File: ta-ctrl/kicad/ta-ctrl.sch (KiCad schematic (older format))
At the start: 6 parts

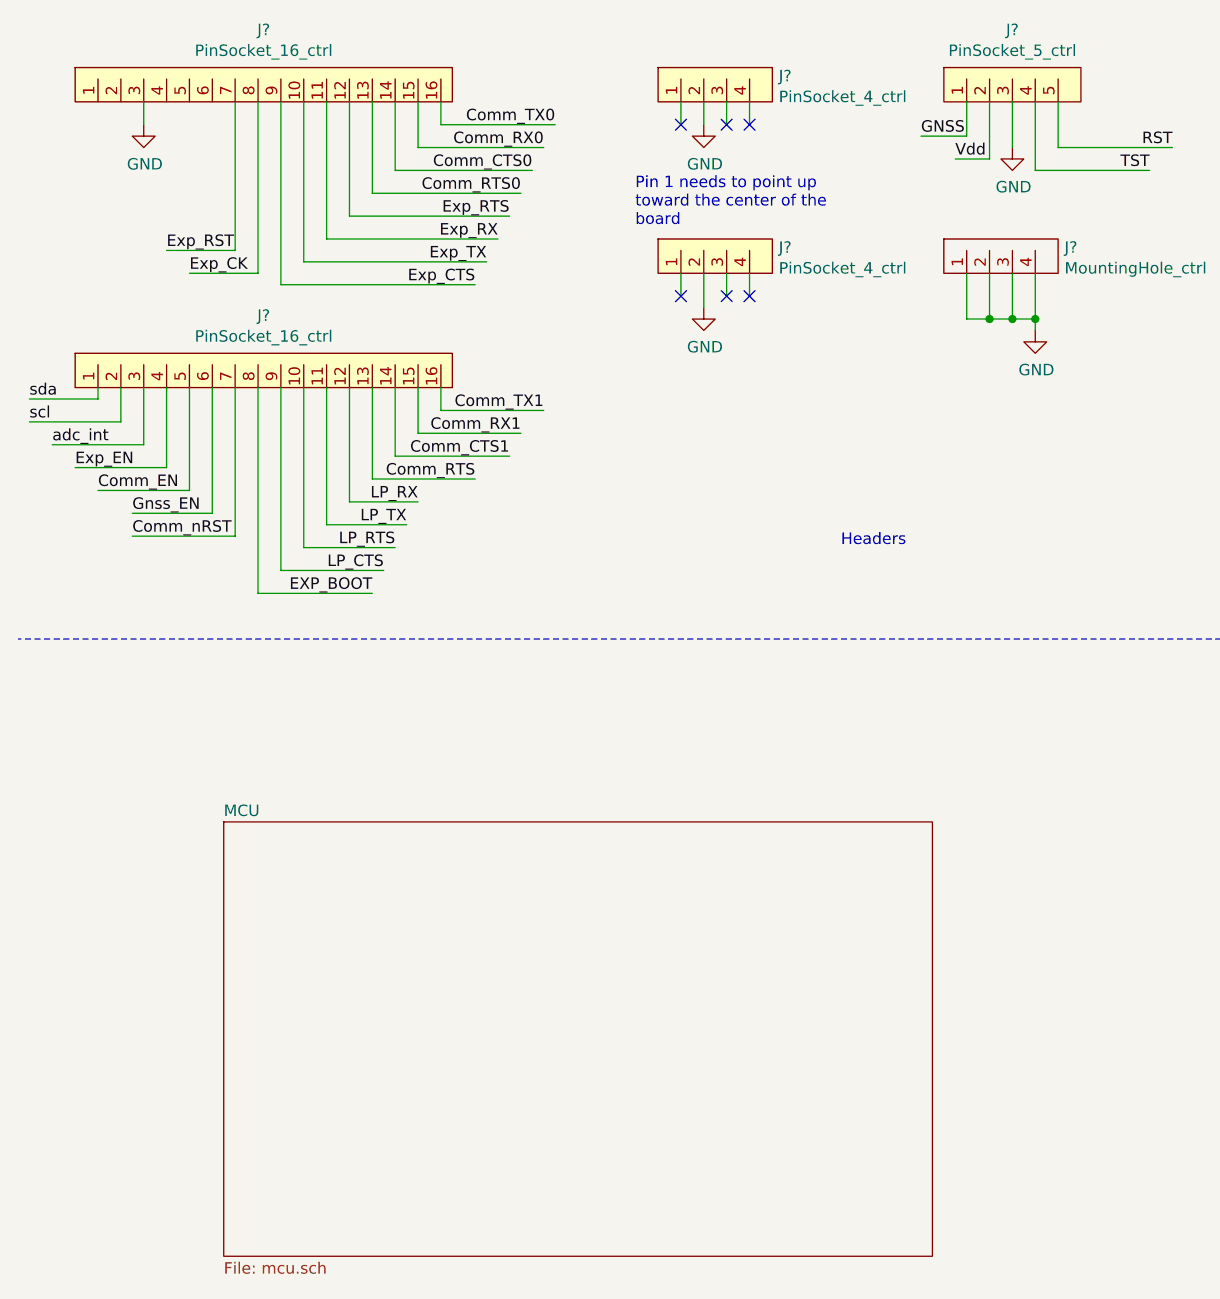
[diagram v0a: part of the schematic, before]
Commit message: Added initial pin assignments
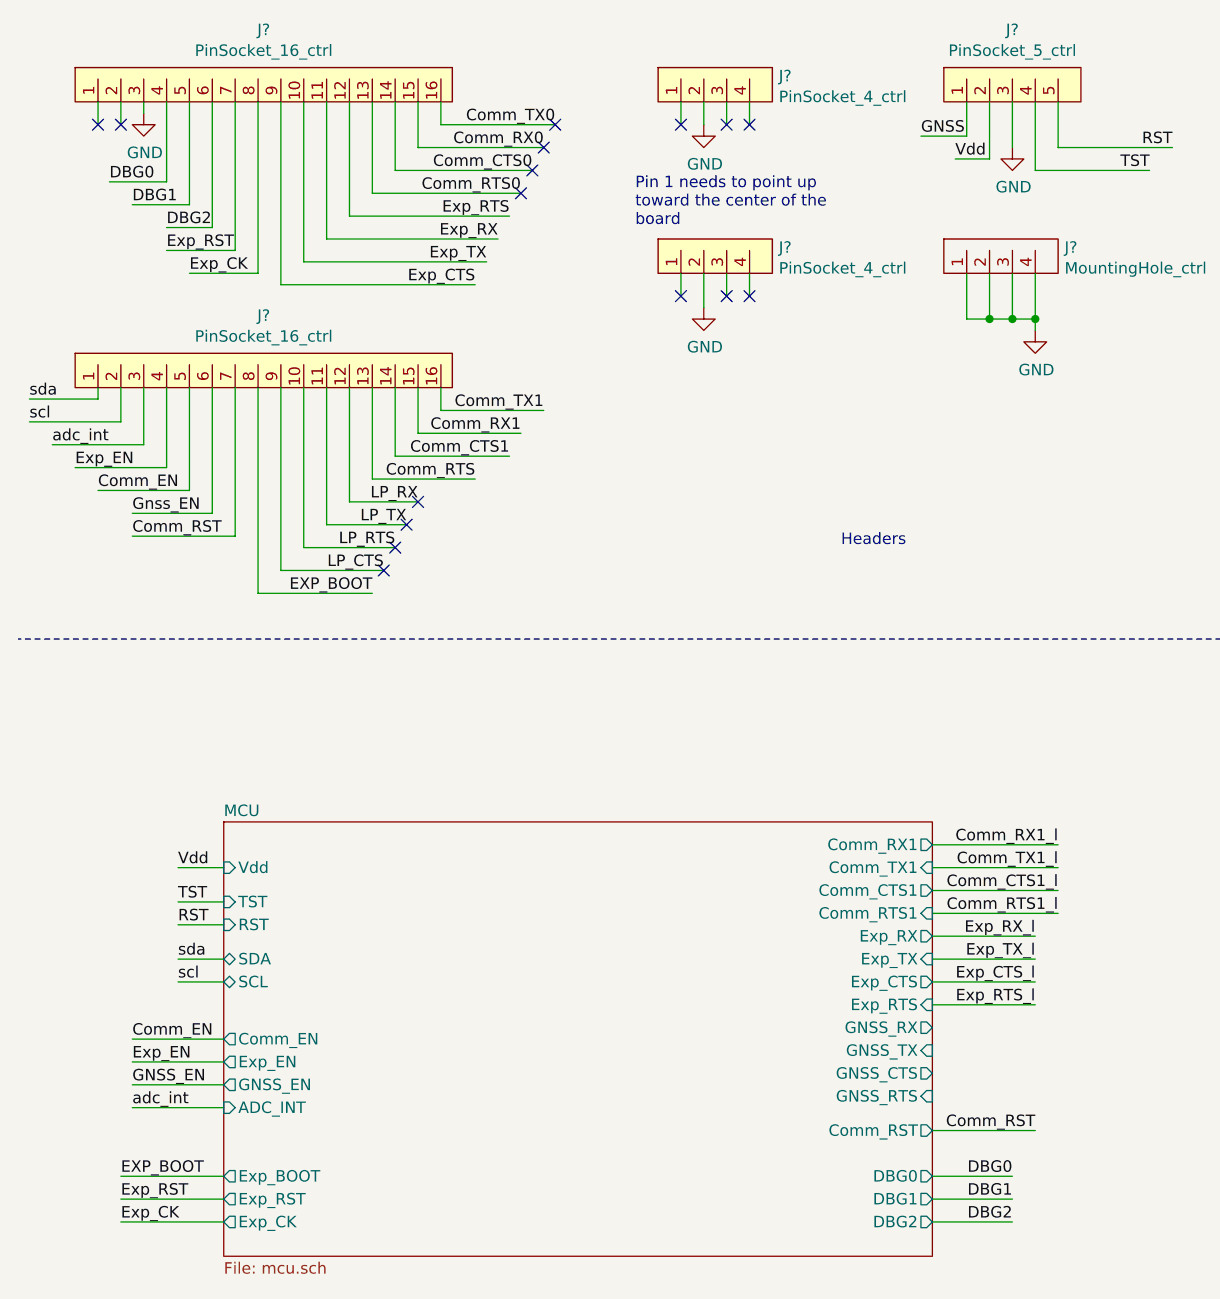
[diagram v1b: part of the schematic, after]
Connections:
- net DBG0: now reaches J?.4
- net DBG1: now reaches J?.5
- net DBG2: now reaches J?.6
- net Comm_nRST renamed Comm_RST
- no-connect marks 6 -> 16
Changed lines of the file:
@@
 	3400 850  3400 950
 Wire Wire Line
-	1050 850  1050 950
+	1050 850  1050 900
 $Comp
 L power:GND #PWR?
 U 1 1 5F17F9A1
-P 1050 950
-F 0 "#PWR?" H 1050 700 50  0001 C CNN
-F 1 "GND" H 1055 777 50  0000 C CNN
-F 2 "" H 1050 950 50  0001 C CNN
-F 3 "" H 1050 950 50  0001 C CNN
-	1    1050 950
+P 1050 900
+F 0 "#PWR?" H 1050 650 50  0001 C CNN
+F 1 "GND" H 1055 727 50  0000 C CNN
+F 2 "" H 1050 900 50  0001 C CNN
+F 3 "" H 1050 900 50  0001 C CNN
+	1    1050 900
 	1    0    0    -1
 $EndComp
@@
 	1450 2100 1450 2750
 Text Label 1000 2750 0    50   ~ 0
-Comm_nRST
+Comm_RST
 Wire Wire Line
 	1000 2750 1450 2750
@@
 Text Label 1250 1600 0    50   ~ 0
 Exp_CK
-Text Label 1150 1500 0    50   ~ 0
-Exp_RST
 Wire Wire Line
 	1550 850  1550 1600
@@
 F0 "MCU" 50
 F1 "mcu.sch" 50
+F2 "Vdd" I L 1400 4200 50
+F3 "TST" I L 1400 4350 50
+F4 "RST" I L 1400 4450 50
+F5 "Comm_RX1" O R 4500 4100 50
+F6 "Comm_TX1" I R 4500 4200 50
+F7 "Exp_RX" O R 4500 4500 50
+F8 "Exp_TX" I R 4500 4600 50
+F9 "Exp_CTS" O R 4500 4700 50
+F10 "Exp_RTS" I R 4500 4800 50
+F11 "GNSS_RX" O R 4500 4900 50
+F12 "GNSS_TX" I R 4500 5000 50
+F13 "GNSS_CTS" O R 4500 5100 50
+F14 "GNSS_RTS" I R 4500 5200 50
+F15 "SDA" B L 1400 4600 50
+F16 "SCL" B L 1400 4700 50
+F17 "Comm_CTS1" O R 4500 4300 50
+F18 "Comm_RTS1" I R 4500 4400 50
+F19 "Comm_EN" O L 1400 4950 50
+F20 "Exp_EN" O L 1400 5050 50
+F21 "GNSS_EN" O L 1400 5150 50
+F22 "ADC_INT" I L 1400 5250 50
+F23 "DBG1" O R 4500 5650 50
+F24 "DBG2" O R 4500 5750 50
+F25 "DBG0" O R 4500 5550 50
+F26 "Exp_BOOT" O L 1400 5550 50
+F27 "Comm_RST" O R 4500 5350 50
+F28 "Exp_CK" O L 1400 5750 50
+F29 "Exp_RST" O L 1400 5650 50
 $EndSheet
 $Sheet
@@
 F1 "sensors.sch" 50
 $EndSheet
+NoConn ~ 2850 950
+NoConn ~ 2800 1050
+NoConn ~ 2750 1150
+NoConn ~ 2700 1250
+NoConn ~ 2250 2600
+NoConn ~ 2200 2700
+NoConn ~ 2150 2800
+NoConn ~ 2100 2900
+Text Label 1200 4200 0    50   ~ 0
+Vdd
+Wire Wire Line
+	1200 4200 1400 4200
+Text Label 5050 4100 2    50   ~ 0
+Comm_RX1_l
+Wire Wire Line
+	4500 4100 5050 4100
+Text Label 5050 4200 2    50   ~ 0
+Comm_TX1_l
+Wire Wire Line
+	4500 4200 5050 4200
+Text Label 5050 4300 2    50   ~ 0
+Comm_CTS1_l
+Text Label 5050 4400 2    50   ~ 0
+Comm_RTS1_l
+Text Label 4950 4500 2    50   ~ 0
+Exp_RX_l
+Text Label 4950 4600 2    50   ~ 0
+Exp_TX_l
+Wire Wire Line
+	4500 4300 5050 4300
+Wire Wire Line
+	4500 4400 5050 4400
+Wire Wire Line
+	4500 4500 4950 4500
+Wire Wire Line
+	4500 4600 4950 4600
+Text Label 4950 4700 2    50   ~ 0
+Exp_CTS_l
+Text Label 4950 4800 2    50   ~ 0
+Exp_RTS_l
+Wire Wire Line
+	4500 4800 4950 4800
+Wire Wire Line
+	4500 4700 4950 4700
+Text Label 1200 4350 0    50   ~ 0
+TST
+Text Label 1200 4450 0    50   ~ 0
+RST
+Text Label 1200 4600 0    50   ~ 0
+sda
+Text Label 1200 4700 0    50   ~ 0
+scl
+Text Label 1000 4950 0    50   ~ 0
+Comm_EN
+Text Label 1000 5050 0    50   ~ 0
+Exp_EN
+Text Label 1000 5150 0    50   ~ 0
+GNSS_EN
+Wire Wire Line
+	1000 4950 1400 4950
+Wire Wire Line
+	1000 5050 1400 5050
+Wire Wire Line
+	1000 5150 1400 5150
+Wire Wire Line
+	1200 4350 1400 4350
+Wire Wire Line
+	1200 4450 1400 4450
+Wire Wire Line
+	1200 4600 1400 4600
+Wire Wire Line
+	1200 4700 1400 4700
+Text Label 1000 5250 0    50   ~ 0
+adc_int
+Wire Wire Line
+	1000 5250 1400 5250
+Text Label 950  5550 0    50   ~ 0
+EXP_BOOT
+Wire Wire Line
+	950  5550 1400 5550
+Text Label 950  5650 0    50   ~ 0
+Exp_RST
+Wire Wire Line
+	950  5650 1400 5650
+Text Label 950  5750 0    50   ~ 0
+Exp_CK
+Wire Wire Line
+	950  5750 1400 5750
+NoConn ~ 850  950
+NoConn ~ 950  950
+Wire Wire Line
+	850  850  850  950
+Wire Wire Line
+	950  850  950  950
+Text Label 900  1200 0    50   ~ 0
+DBG0
+Text Label 1000 1300 0    50   ~ 0
+DBG1
+Text Label 1150 1400 0    50   ~ 0
+DBG2
+Text Label 1150 1500 0    50   ~ 0
+Exp_RST
+Wire Wire Line
+	1350 850  1350 1400
+Wire Wire Line
+	1350 1400 1150 1400
+Wire Wire Line
+	1250 850  1250 1300
+Wire Wire Line
+	1250 1300 1000 1300
+Wire Wire Line
+	1150 850  1150 1200
+Wire Wire Line
+	1150 1200 900  1200
+Wire Wire Line
+	4500 5350 4950 5350
+Text Label 4950 5350 2    50   ~ 0
+Comm_RST
+Text Label 4850 5550 2    50   ~ 0
+DBG0
+Text Label 4850 5650 2    50   ~ 0
+DBG1
+Text Label 4850 5750 2    50   ~ 0
+DBG2
+Wire Wire Line
+	4500 5550 4850 5550
+Wire Wire Line
+	4500 5650 4850 5650
+Wire Wire Line
+	4500 5750 4850 5750
 $EndSCHEMATC

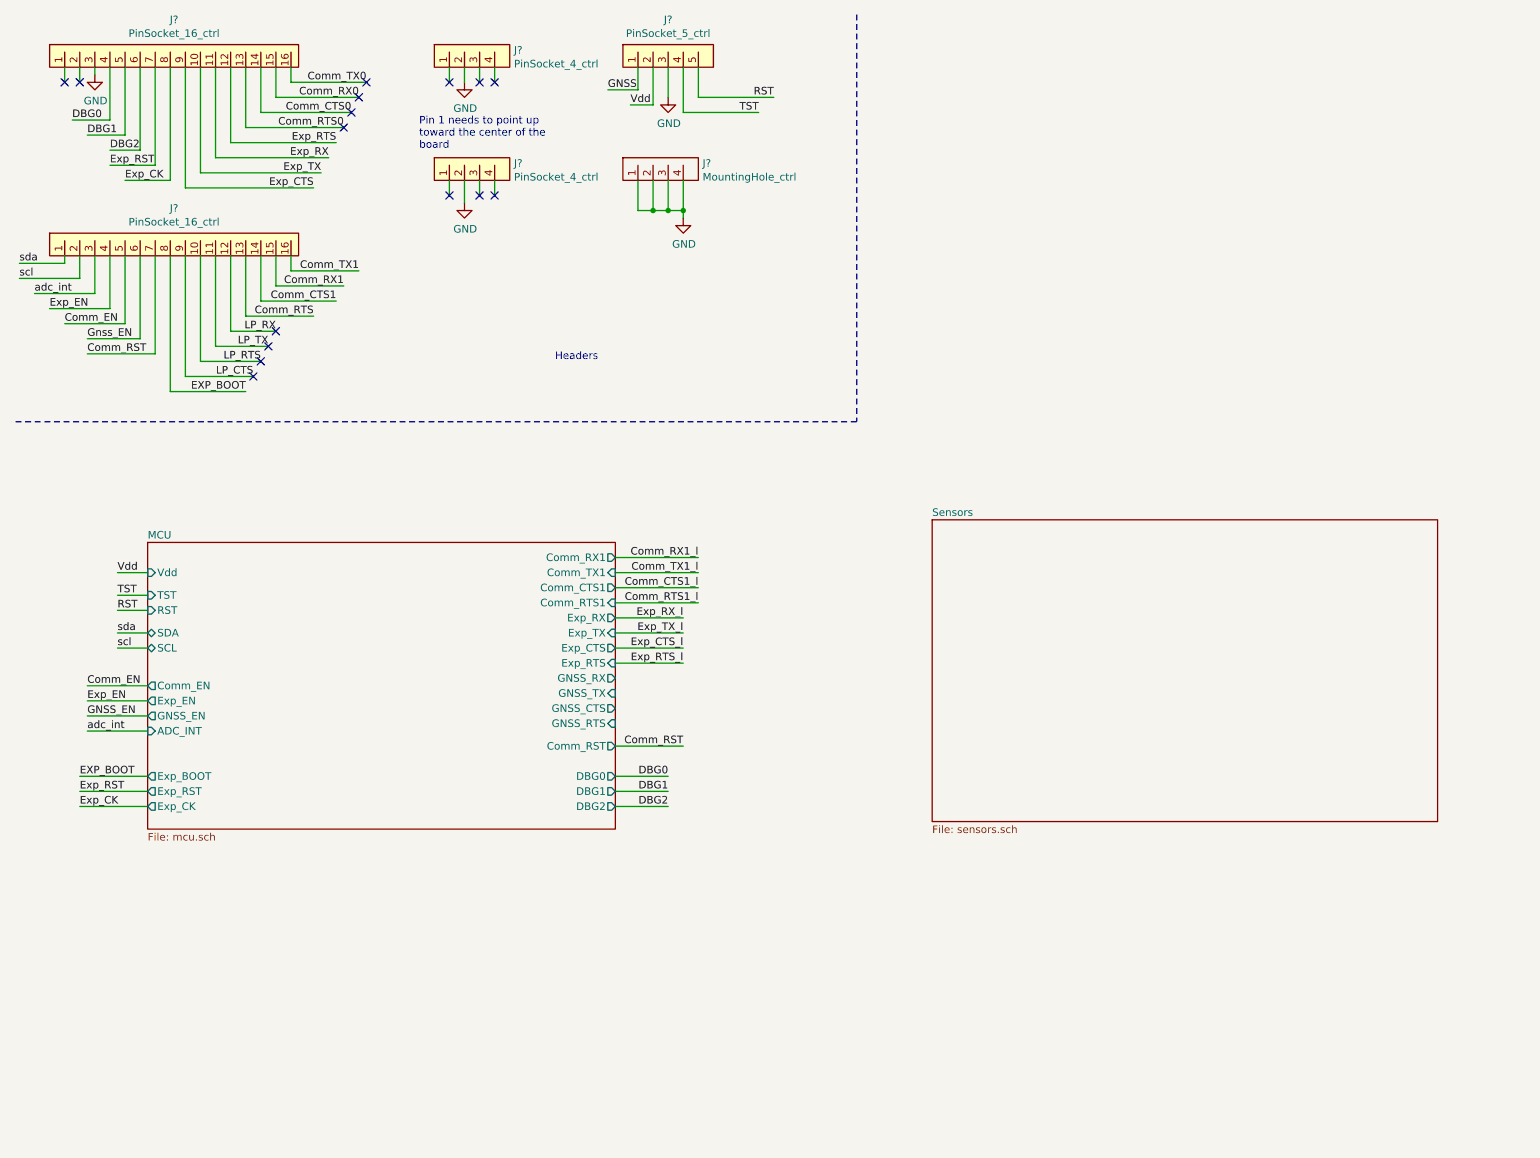
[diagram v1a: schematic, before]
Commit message: level shifters wired in, need to finalize connections between MCU and sensors
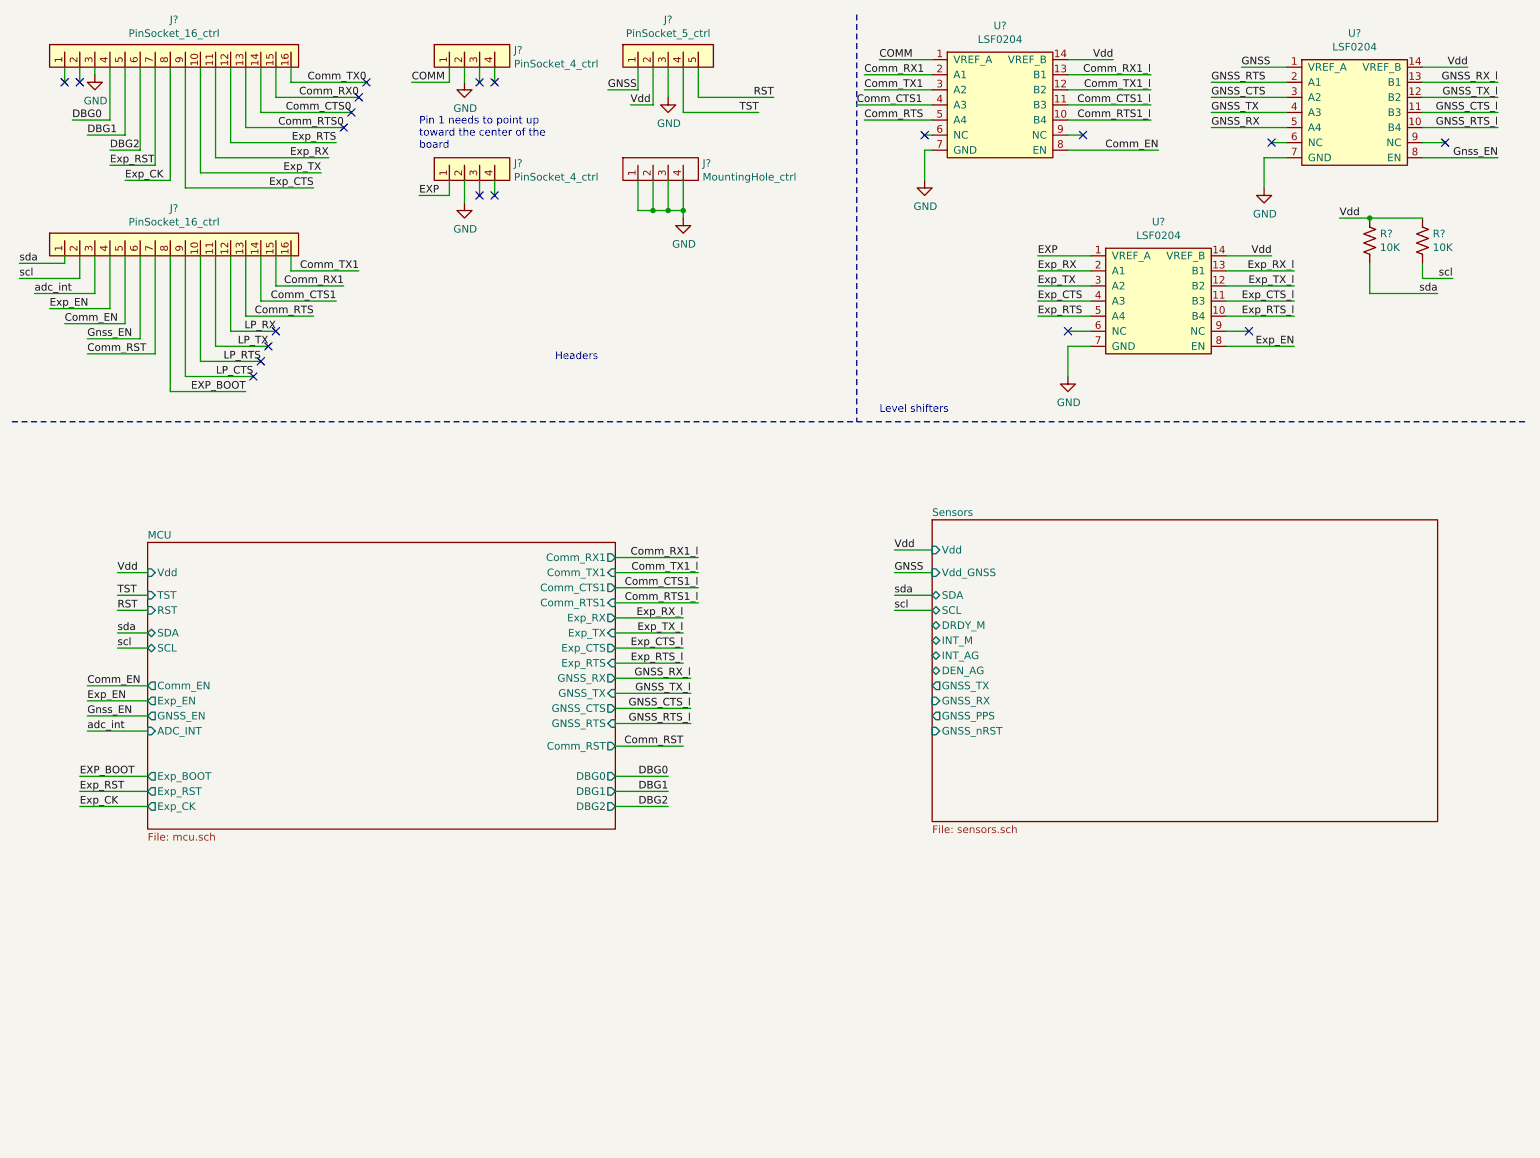
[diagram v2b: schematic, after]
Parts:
- added R? (x2): 10K, symbol Device:R_US
- added U? (x3): LSF0204, symbol ta-ctrl:LSF0204
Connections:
- net Comm_CTS1: now also U?.4 (A3)
- net Comm_CTS1_l: now also U?.11 (B3)
- net Comm_EN: now also U?.8 (EN)
- net Comm_RTS: now also U?.5 (A4)
- net Comm_RTS1_l: now also U?.10 (B4)
- net Comm_RX1: now also U?.2 (A1)
- net Comm_RX1_l: now also U?.13 (B1)
- net Comm_TX1: now also U?.3 (A2)
- net Comm_TX1_l: now also U?.12 (B2)
- net Exp_CTS: now also U?.4 (A3)
- net Exp_CTS_l: now also U?.11 (B3)
- net Exp_EN: now also U?.8 (EN)
- net Exp_RTS: now also U?.5 (A4)
- net Exp_RTS_l: now also U?.10 (B4)
- net Exp_RX: now also U?.2 (A1)
- net Exp_RX_l: now also U?.13 (B1)
- net Exp_TX: now also U?.3 (A2)
- net Exp_TX_l: now also U?.12 (B2)
- net GND: now also U?.7 (GND), U?.7 (GND), U?.7 (GND)
- net GNSS: now also U?.1 (VREF_A)
- net Gnss_EN: now also U?.8 (EN)
- net Vdd: now also R?.1, R?.1, U?.14 (VREF_B), U?.14 (VREF_B), U?.14 (VREF_B)
- net scl: now also R?.2
- net sda: now also R?.2
- net COMM: now reaches J?.1
- net COMM: now also U?.1 (VREF_A)
- net EXP: now reaches J?.1
- net EXP: now also U?.1 (VREF_A)
- new net GNSS_CTS: U?.3 (A2)
- new net GNSS_CTS_l: U?.11 (B3)
- new net GNSS_RTS: U?.2 (A1)
- new net GNSS_RTS_l: U?.10 (B4)
- new net GNSS_RX: U?.5 (A4)
- new net GNSS_RX_l: U?.13 (B1)
- new net GNSS_TX: U?.4 (A3)
- new net GNSS_TX_l: U?.12 (B2)
- no-connect marks 16 -> 20
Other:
- note added: "Level shifters"

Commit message: finalized connections to MCU
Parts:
- added J7: PinSocket_5_ctrl, ta-ctrl:PinSocket_1x5_right_TartanArtibeus_ctrl_cpy, symbol ta-ctrl:PinSocket_5_ctrl
- added R1, R10, R11, R12, R2, R3, R4, R5, R6, R7, R8, R9: DNP, symbol Device:R_US
- gave numbers to parts that had none: 11
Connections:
- net GNSS_CTS_l is gone; now on net GNSS_TX_l: U3.11 (B3)
- net GNSS_RTS_l is gone; now on net GNSS_RX_l: U3.10 (B4)
- net Comm_CTS1: now also R3.2
- net Comm_CTS1_l: now also R3.1
- net Comm_RTS: now also R4.2
- net Comm_RTS1_l: now also R4.1
- net Comm_RX1: now also R1.2
- net Comm_RX1_l: now also R1.1
- net Comm_TX1: now also R2.2
- net Comm_TX1_l: now also R2.1
- net Exp_CTS: now also R7.2
- net Exp_CTS_l: now also R7.1
- net Exp_RTS: now also R8.2
- net Exp_RTS_l: now also R8.1
- net Exp_RX: now also R5.2
- net Exp_RX_l: now also R5.1
- net Exp_TX: now also R6.2
- net Exp_TX_l: now also R6.1
- net GNSS_RX: now also R12.2
- net GNSS_RX_l: now also R12.1; no longer U3.13 (B1)
- net GNSS_TX: now also R11.2
- net GNSS_TX_l: now also R11.1; no longer U3.12 (B2)
- net GNSS_CTS renamed GNSS_nRST
- net GNSS_nRST: now also R10.2
- net GNSS_RTS renamed GNSS_PPS
- net GNSS_PPS: now also R9.2
- new net GNSS_PPS_l: R9.1, U3.13 (B1)
- new net GNSS_nRST_l: R10.1, U3.12 (B2)
- no-connect marks 20 -> 25
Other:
- note added: "DNP resistors for\nbypassing level \nshifters"
- moved on the sheet: J3

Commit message: more footprints, changed symbol library path
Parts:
- J7: footprint ta-ctrl:PinSocket_1x5_right_TartanArtibeus_ctrl_cpy -> ta-ctrl:PinSocket_1x5_left_TartanArtibeus_ctrl_cpy
- U1, U2, U3: footprint (none) -> ta-ctrl:TSSOP-14
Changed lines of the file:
@@
 Date "2020-07-21"
 Rev "v0"
-Comp "Carnegie Mellon University"
+Comp "Carnegie Mellon University -- Emily Ruppel"
 Comment1 ""
 Comment2 ""
@@
 F 0 "U1" H 7050 1825 50  0000 C CNN
 F 1 "LSF0204" H 7050 1734 50  0000 C CNN
-F 2 "" H 6850 1200 50  0001 C CNN
+F 2 "ta-ctrl:TSSOP-14" H 6850 1200 50  0001 C CNN
 F 3 "" H 6850 1200 50  0001 C CNN
 	1    7050 1200
@@
 F 0 "U3" H 9400 1875 50  0000 C CNN
 F 1 "LSF0204" H 9400 1784 50  0000 C CNN
-F 2 "" H 9200 1250 50  0001 C CNN
+F 2 "ta-ctrl:TSSOP-14" H 9200 1250 50  0001 C CNN
 F 3 "" H 9200 1250 50  0001 C CNN
 	1    9400 1250
@@
 F 0 "U2" H 8100 3125 50  0000 C CNN
 F 1 "LSF0204" H 8100 3034 50  0000 C CNN
-F 2 "" H 7900 2500 50  0001 C CNN
+F 2 "ta-ctrl:TSSOP-14" H 7900 2500 50  0001 C CNN
 F 3 "" H 7900 2500 50  0001 C CNN
 	1    8100 2500
@@
 F 0 "J7" H 4850 2915 50  0000 C CNN
 F 1 "PinSocket_5_ctrl" H 4850 2824 50  0000 C CNN
-F 2 "ta-ctrl:PinSocket_1x5_right_TartanArtibeus_ctrl_cpy" H 4750 2600 50  0001 C CNN
+F 2 "ta-ctrl:PinSocket_1x5_left_TartanArtibeus_ctrl_cpy" H 4750 2600 50  0001 C CNN
 F 3 "" H 4750 2600 50  0001 C CNN
 	1    4850 2600
